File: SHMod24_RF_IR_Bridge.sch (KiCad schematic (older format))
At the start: 4 parts, among them J1 Conn_02x14_Odd_Even

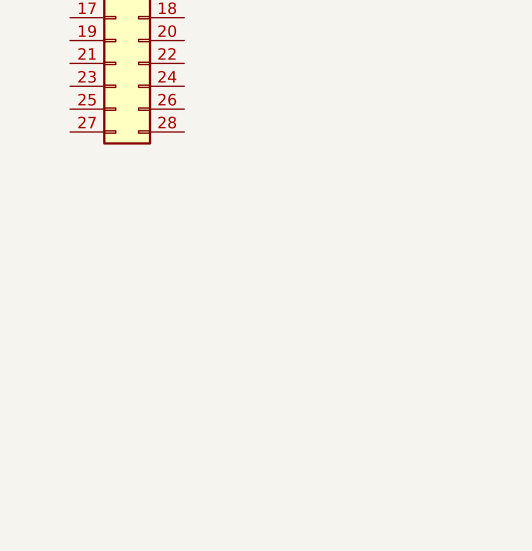
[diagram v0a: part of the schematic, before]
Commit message: add smd pin header option
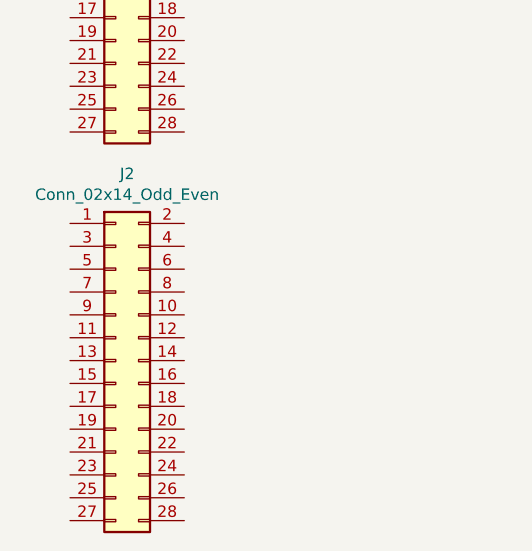
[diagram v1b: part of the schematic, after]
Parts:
- added J2: Conn_02x14_Odd_Even, Connector_PinSocket_2.54mm:PinSocket_2x14_P2.54mm_Vertical_SMD, symbol Connector_Generic:Conn_02x14_Odd_Even
- J1: footprint leodj-kicad:PinSocket_2x14_P2.54mm_Vertical -> LeoDJ-kicad:PinSocket_2x14_P2.54mm_Vertical
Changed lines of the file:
@@
 F 0 "J1" H 1850 4667 50  0000 C CNN
 F 1 "Conn_02x14_Odd_Even" H 1850 4576 50  0000 C CNN
-F 2 "leodj-kicad:PinSocket_2x14_P2.54mm_Vertical" H 1800 3850 50  0001 C CNN
+F 2 "LeoDJ-kicad:PinSocket_2x14_P2.54mm_Vertical" H 1800 3850 50  0001 C CNN
 F 3 "~" H 1800 3850 50  0001 C CNN
 	1    1800 3850
 	1    0    0    -1
 $EndComp
+$Comp
+L Connector_Generic:Conn_02x14_Odd_Even J2
+U 1 1 5C3E7240
+P 1800 5550
+F 0 "J2" H 1850 6367 50  0000 C CNN
+F 1 "Conn_02x14_Odd_Even" H 1850 6276 50  0000 C CNN
+F 2 "Connector_PinSocket_2.54mm:PinSocket_2x14_P2.54mm_Vertical_SMD" H 1800 5550 50  0001 C CNN
+F 3 "~" H 1800 5550 50  0001 C CNN
+	1    1800 5550
+	1    0    0    -1
+$EndComp

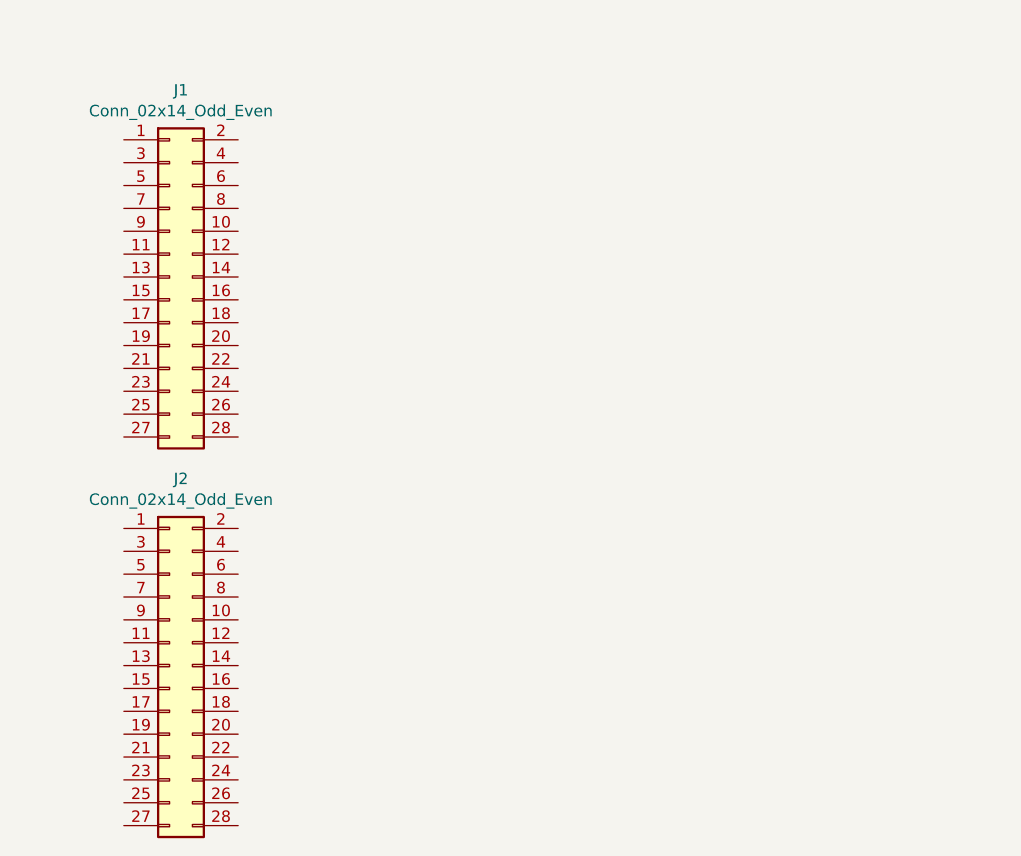
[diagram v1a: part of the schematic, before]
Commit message: design IR send / receive
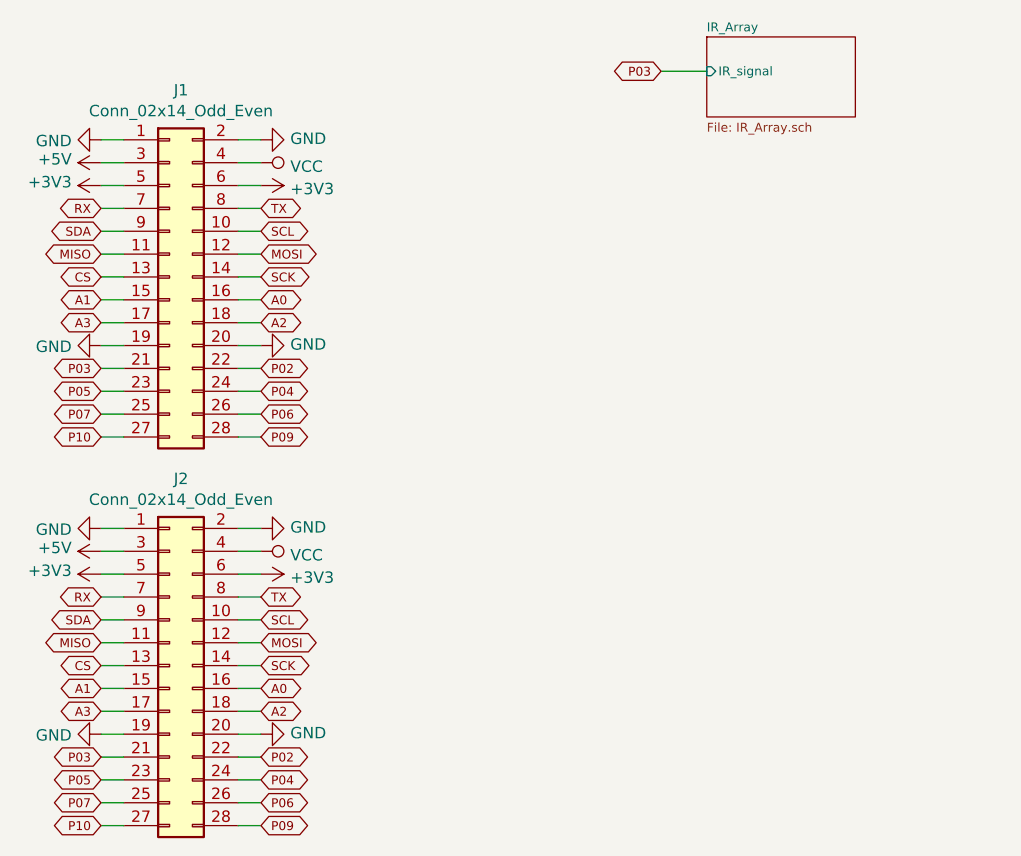
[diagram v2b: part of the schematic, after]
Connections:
- net GND: now reaches J1.1 (Pin_1)
- net GND: now also J1.19 (Pin_19), J1.2 (Pin_2), J1.20 (Pin_20), J2.1 (Pin_1), J2.19 (Pin_19), J2.2 (Pin_2), J2.20 (Pin_20)
- net SCL: now reaches J1.10 (Pin_10)
- net SCL: now also J2.10 (Pin_10)
- net MISO: now reaches J1.11 (Pin_11)
- net MISO: now also J2.11 (Pin_11)
- net MOSI: now reaches J1.12 (Pin_12)
- net MOSI: now also J2.12 (Pin_12)
- net CS: now reaches J1.13 (Pin_13)
- net CS: now also J2.13 (Pin_13)
- net SCK: now reaches J1.14 (Pin_14)
- net SCK: now also J2.14 (Pin_14)
- net A1: now reaches J1.15 (Pin_15)
- net A1: now also J2.15 (Pin_15)
- net A0: now reaches J1.16 (Pin_16)
- net A0: now also J2.16 (Pin_16)
- net A3: now reaches J1.17 (Pin_17)
- net A3: now also J2.17 (Pin_17)
- net A2: now reaches J1.18 (Pin_18)
- net A2: now also J2.18 (Pin_18)
- net P03: now reaches J1.21 (Pin_21)
- net P03: now also J2.21 (Pin_21)
- net P02: now reaches J1.22 (Pin_22)
- net P02: now also J2.22 (Pin_22)
- net P05: now reaches J1.23 (Pin_23)
- net P05: now also J2.23 (Pin_23)
- net P04: now reaches J1.24 (Pin_24)
- net P04: now also J2.24 (Pin_24)
- net P07: now reaches J1.25 (Pin_25)
- net P07: now also J2.25 (Pin_25)
- net P06: now reaches J1.26 (Pin_26)
- net P06: now also J2.26 (Pin_26)
- net P10: now reaches J1.27 (Pin_27)
- net P10: now also J2.27 (Pin_27)
- net P09: now reaches J1.28 (Pin_28)
- net P09: now also J2.28 (Pin_28)
- net +5V: now reaches J1.3 (Pin_3)
- net +5V: now also J2.3 (Pin_3)
- net VCC: now reaches J1.4 (Pin_4)
- net VCC: now also J2.4 (Pin_4)
- net +3V3: now reaches J1.5 (Pin_5)
- net +3V3: now also J1.6 (Pin_6), J2.5 (Pin_5), J2.6 (Pin_6)
- net RX: now reaches J1.7 (Pin_7)
- net RX: now also J2.7 (Pin_7)
- net TX: now reaches J1.8 (Pin_8)
- net TX: now also J2.8 (Pin_8)
- net SDA: now reaches J1.9 (Pin_9)
- net SDA: now also J2.9 (Pin_9)

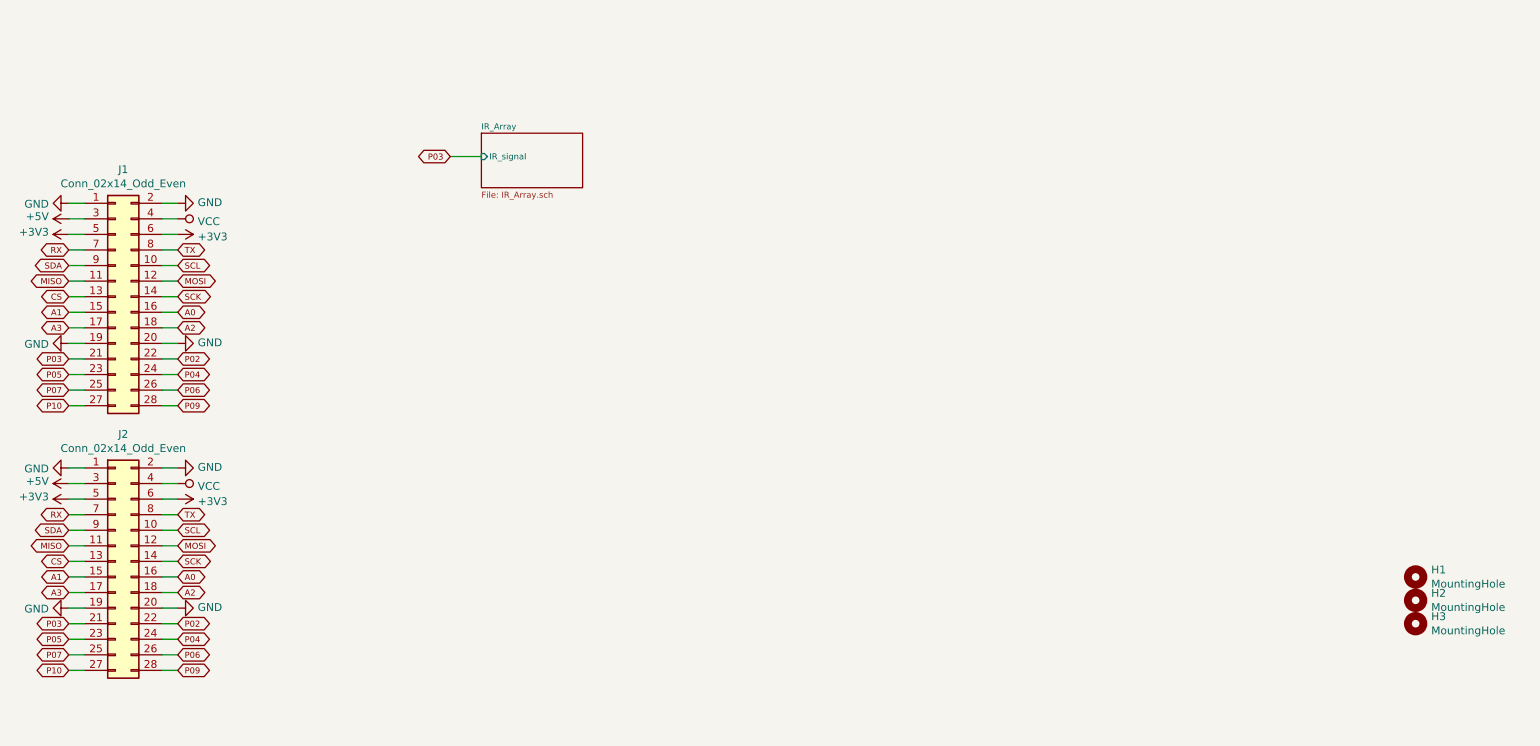
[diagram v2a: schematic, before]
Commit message: add boost converter, IR RX, 433MHz RX/TX and labels
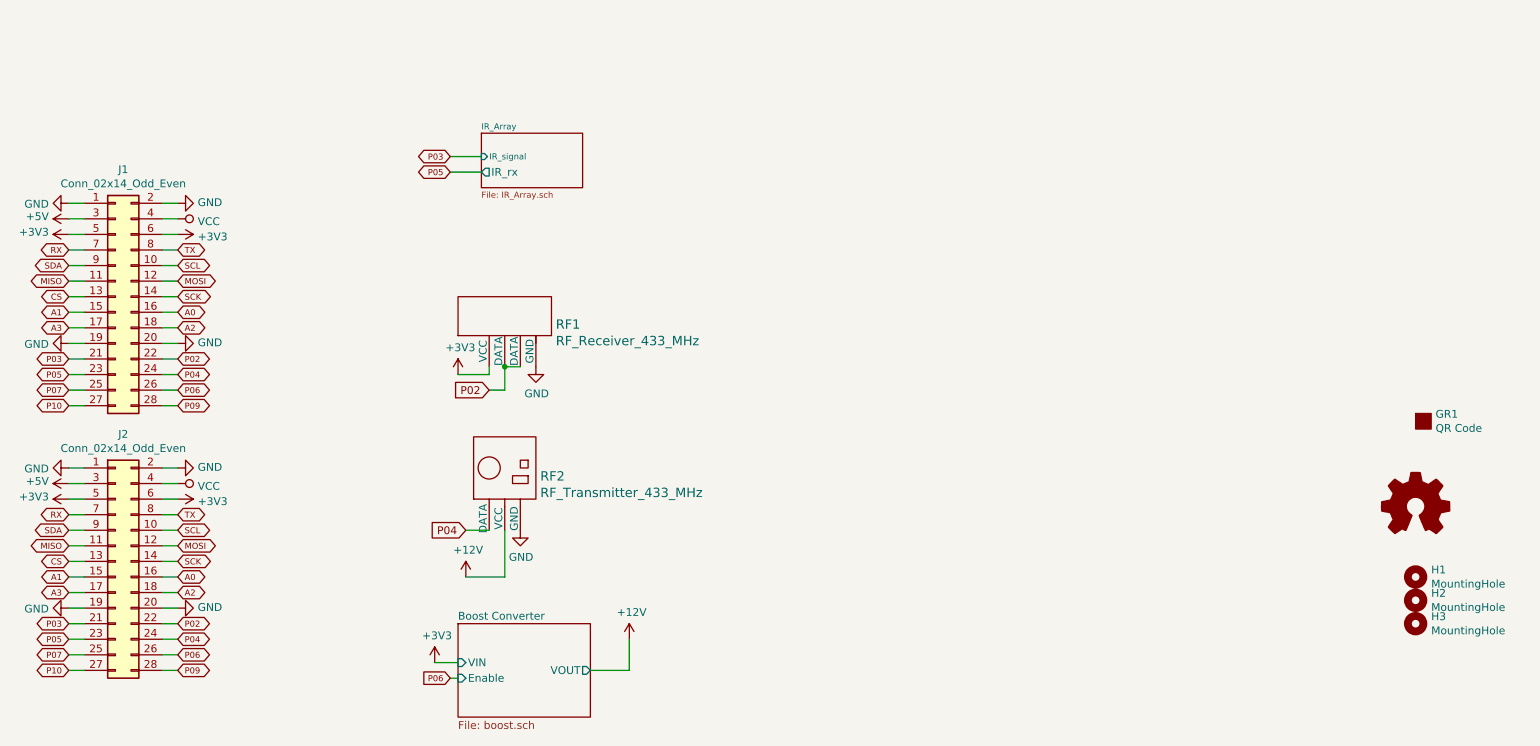
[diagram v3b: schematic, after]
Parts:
- added GR1: QR Code, LeoDJ-kicad:QR_Code_SHMod24-IRRF, symbol LeoDJ-kicad:GenericGraphic
- added LOGO1: Logo_Open_Hardware_Small, Symbol:OSHW-Logo2_7.3x6mm_SilkScreen, symbol Graphic:Logo_Open_Hardware_Small
- added RF1: RF_Receiver_433_MHz, LeoDJ-kicad:RF_Receiver_433_MHz, symbol LeoDJ-kicad:RF_Receiver_433_MHz
- added RF2: RF_Transmitter_433_MHz, LeoDJ-kicad:RF_Transmitter_433_MHz, symbol LeoDJ-kicad:RF_Transmitter_433_MHz
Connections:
- net +3V3: now also RF1.1 (VCC)
- net GND: now also RF1.4 (GND), RF2.3 (GND)
- net P02: now also RF1.2 (DATA), RF1.3 (DATA)
- net P04: now also RF2.1 (DATA)
- new net +12V: RF2.2 (VCC)
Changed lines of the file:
@@
 $Descr A4 11693 8268
 encoding utf-8
-Sheet 1 2
+Sheet 1 3
 Title ""
 Date ""
@@
 F1 "IR_Array.sch" 39
 F2 "IR_signal" I L 4150 2950 39
+F3 "IR_rx" O L 4150 3050 50
 $EndSheet
 Text GLabel 3950 2950 0    39   BiDi ~ 0
@@
 Wire Wire Line
 	3950 2950 4150 2950
+Text GLabel 3950 3050 0    39   BiDi ~ 0
+P05
+Wire Wire Line
+	3950 3050 4150 3050
+$Comp
+L LeoDJ-kicad:RF_Receiver_433_MHz RF1
+U 1 1 5C424CB0
+P 4300 4300
+F 0 "RF1" H 4628 4572 60  0000 L CNN
+F 1 "RF_Receiver_433_MHz" H 4628 4466 60  0000 L CNN
+F 2 "LeoDJ-kicad:RF_Receiver_433_MHz" H 4400 4300 60  0001 C CNN
+F 3 "" H 4400 4300 60  0000 C CNN
+	1    4300 4300
+	1    0    0    -1
+$EndComp
+$Comp
+L LeoDJ-kicad:RF_Transmitter_433_MHz RF2
+U 1 1 5C424E16
+P 4300 5350
+F 0 "RF2" H 4528 5697 60  0000 L CNN
+F 1 "RF_Transmitter_433_MHz" H 4528 5591 60  0000 L CNN
+F 2 "LeoDJ-kicad:RF_Transmitter_433_MHz" H 4300 5350 60  0001 C CNN
+F 3 "" H 4300 5350 60  0000 C CNN
+	1    4300 5350
+	1    0    0    -1
+$EndComp
+$Comp
+L power:GND #PWR0129
+U 1 1 5C424EB4
+P 4500 4300
+F 0 "#PWR0129" H 4500 4050 50  0001 C CNN
+F 1 "GND" H 4505 4127 50  0000 C CNN
+F 2 "" H 4500 4300 50  0001 C CNN
+F 3 "" H 4500 4300 50  0001 C CNN
+	1    4500 4300
+	1    0    0    -1
+$EndComp
+$Comp
+L power:GND #PWR0130
+U 1 1 5C424EF2
+P 4400 5350
+F 0 "#PWR0130" H 4400 5100 50  0001 C CNN
+F 1 "GND" H 4405 5177 50  0000 C CNN
+F 2 "" H 4400 5350 50  0001 C CNN
+F 3 "" H 4400 5350 50  0001 C CNN
+	1    4400 5350
+	1    0    0    -1
+$EndComp
+$Comp
+L power:+3V3 #PWR0131
+U 1 1 5C424F37
+P 4000 4350
+F 0 "#PWR0131" H 4000 4200 50  0001 C CNN
+F 1 "+3V3" H 4015 4523 50  0000 C CNN
+F 2 "" H 4000 4350 50  0001 C CNN
+F 3 "" H 4000 4350 50  0001 C CNN
+	1    4000 4350
+	1    0    0    -1
+$EndComp
+Wire Wire Line
+	4200 4300 4200 4350
+Wire Wire Line
+	4200 4350 4000 4350
+Text GLabel 4200 4450 0    50   Input ~ 0
+P02
+Wire Wire Line
+	4200 4450 4300 4450
+Wire Wire Line
+	4300 4450 4300 4300
+Wire Wire Line
+	4300 4300 4400 4300
+Connection ~ 4300 4300
+Text GLabel 4050 5350 0    50   Input ~ 0
+P04
+Wire Wire Line
+	4050 5350 4200 5350
+$Sheet
+S 4000 5950 850  600
+U 5C50C113
+F0 "Boost Converter" 50
+F1 "boost.sch" 50
+F2 "VIN" I L 4000 6200 50
+F3 "VOUT" O R 4850 6250 50
+F4 "Enable" I L 4000 6300 50
+$EndSheet
+$Comp
+L power:+12V #PWR0136
+U 1 1 5C50FE3A
+P 5100 6050
+F 0 "#PWR0136" H 5100 5900 50  0001 C CNN
+F 1 "+12V" H 5115 6223 50  0000 C CNN
+F 2 "" H 5100 6050 50  0001 C CNN
+F 3 "" H 5100 6050 50  0001 C CNN
+	1    5100 6050
+	1    0    0    -1
+$EndComp
+Wire Wire Line
+	4850 6250 5100 6250
+Wire Wire Line
+	5100 6250 5100 6050
+$Comp
+L power:+12V #PWR0137
+U 1 1 5C5160C1
+P 4050 5650
+F 0 "#PWR0137" H 4050 5500 50  0001 C CNN
+F 1 "+12V" H 4065 5823 50  0000 C CNN
+F 2 "" H 4050 5650 50  0001 C CNN
+F 3 "" H 4050 5650 50  0001 C CNN
+	1    4050 5650
+	1    0    0    -1
+$EndComp
+Wire Wire Line
+	4050 5650 4300 5650
+Wire Wire Line
+	4300 5650 4300 5350
+$Comp
+L power:+3V3 #PWR0123
+U 1 1 5C51C62A
+P 3850 6200
+F 0 "#PWR0123" H 3850 6050 50  0001 C CNN
+F 1 "+3V3" H 3865 6373 50  0000 C CNN
+F 2 "" H 3850 6200 50  0001 C CNN
+F 3 "" H 3850 6200 50  0001 C CNN
+	1    3850 6200
+	1    0    0    -1
+$EndComp
+Wire Wire Line
+	3850 6200 4000 6200
+Text GLabel 3950 6300 0    39   Input ~ 0
+P06
+Wire Wire Line
+	4000 6300 3950 6300
+$Comp
+L Graphic:Logo_Open_Hardware_Small LOGO1
+U 1 1 5C523CB2
+P 10150 5200
+F 0 "LOGO1" H 10150 5475 50  0001 C CNN
+F 1 "Logo_Open_Hardware_Small" H 10150 4975 50  0001 C CNN
+F 2 "Symbol:OSHW-Logo2_7.3x6mm_SilkScreen" H 10150 5200 50  0001 C CNN
+F 3 "~" H 10150 5200 50  0001 C CNN
+	1    10150 5200
+	1    0    0    -1
+$EndComp
+$Comp
+L LeoDJ-kicad:GenericGraphic GR1
+U 1 1 5C522029
+P 10200 4650
+F 0 "GR1" H 10278 4696 50  0000 L CNN
+F 1 "QR Code" H 10278 4605 50  0000 L CNN
+F 2 "LeoDJ-kicad:QR_Code_SHMod24-IRRF" H 10200 4650 50  0001 C CNN
+F 3 "" H 10200 4650 50  0001 C CNN
+	1    10200 4650
+	1    0    0    -1
+$EndComp
 $EndSCHEMATC

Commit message: add serial comms header
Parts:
- added J3: Conn_01x06, Connector_PinHeader_2.54mm:PinHeader_1x06_P2.54mm_Vertical, symbol Connector_Generic:Conn_01x06
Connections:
- net +3V3: now also J3.3 (Pin_3)
- net GND: now also J3.1 (Pin_1), J3.2 (Pin_2)
- net RX: now also J3.4 (Pin_4)
- net TX: now also J3.5 (Pin_5)
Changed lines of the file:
@@
 	1    0    0    -1
 $EndComp
+$Comp
+L Connector_Generic:Conn_01x06 J3
+U 1 1 5C522FC9
+P 1850 2600
+F 0 "J3" H 1770 2075 50  0000 C CNN
+F 1 "Conn_01x06" H 1770 2166 50  0000 C CNN
+F 2 "Connector_PinHeader_2.54mm:PinHeader_1x06_P2.54mm_Vertical" H 1850 2600 50  0001 C CNN
+F 3 "~" H 1850 2600 50  0001 C CNN
+	1    1850 2600
+	-1   0    0    1
+$EndComp
+$Comp
+L power:GND #PWR0140
+U 1 1 5C5230B9
+P 2050 2800
+F 0 "#PWR0140" H 2050 2550 50  0001 C CNN
+F 1 "GND" V 2055 2672 50  0000 R CNN
+F 2 "" H 2050 2800 50  0001 C CNN
+F 3 "" H 2050 2800 50  0001 C CNN
+	1    2050 2800
+	0    -1   -1   0
+$EndComp
+$Comp
+L power:+3V3 #PWR0141
+U 1 1 5C523102
+P 2050 2600
+F 0 "#PWR0141" H 2050 2450 50  0001 C CNN
+F 1 "+3V3" V 2065 2728 50  0000 L CNN
+F 2 "" H 2050 2600 50  0001 C CNN
+F 3 "" H 2050 2600 50  0001 C CNN
+	1    2050 2600
+	0    1    1    0
+$EndComp
+$Comp
+L power:GND #PWR0142
+U 1 1 5C52990C
+P 2050 2700
+F 0 "#PWR0142" H 2050 2450 50  0001 C CNN
+F 1 "GND" V 2055 2572 50  0000 R CNN
+F 2 "" H 2050 2700 50  0001 C CNN
+F 3 "" H 2050 2700 50  0001 C CNN
+	1    2050 2700
+	0    -1   -1   0
+$EndComp
+Text GLabel 2050 2500 2    39   BiDi ~ 0
+RX
+Text GLabel 2050 2400 2    39   BiDi ~ 0
+TX
 $EndSCHEMATC

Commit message: final touches
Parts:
- added GR2: NightFury, LeoDJ-kicad:NightFury_Roll_8.0x6.1, symbol LeoDJ-kicad:GenericGraphic
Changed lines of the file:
@@
 Text GLabel 2050 2400 2    39   BiDi ~ 0
 TX
+$Comp
+L LeoDJ-kicad:GenericGraphic GR2
+U 1 1 5C52CE28
+P 10200 4400
+F 0 "GR2" H 10278 4446 50  0000 L CNN
+F 1 "NightFury" H 10278 4355 50  0000 L CNN
+F 2 "LeoDJ-kicad:NightFury_Roll_8.0x6.1" H 10200 4400 50  0001 C CNN
+F 3 "" H 10200 4400 50  0001 C CNN
+	1    10200 4400
+	1    0    0    -1
+$EndComp
 $EndSCHEMATC
